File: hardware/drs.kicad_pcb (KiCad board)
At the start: 4 copper layers, 70 x 45 mm, 100 parts, among them IC1 TPS54202HDDCR, J1 USB_C_Receptacle_USB2.0_16P, J2 FTSH-107-01-L-D-K, J3 POWER & CAN & SPI2, J4 PWM1, J5 PWM2, Q1 SI2347DS-T1-GE3, Q2 LMR51635XDDCR, Q3 LMR51635XDDCR, T1 TP_VCC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

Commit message: pcb can & usb update
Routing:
- net /Control/NRST: track 14.9 -> 16.3 mm
- net /Connectors/TX: track 19.0 -> 20.5 mm
- net GND: track 27.6 -> 26.5 mm

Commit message: pcb update
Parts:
- moved J3 13.4 mm to (141.8, 74.8), turned to 180 degrees
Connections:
- J3 pad 10: /Connectors/SCK -> CAN_P
- J3 pad 11: GND -> unconnected-(J3-Pin_11-Pad11)
- J3 pad 12: GND -> CAN_N
- J3 pad 3: +6V6S1 -> GND
- J3 pad 4: CAN_L -> GND
- J3 pad 5: +6V6S2 -> /Connectors/SCK
- J3 pad 6: CAN_H -> /Connectors/MISO
- J3 pad 7: /Connectors/MISO -> unconnected-(J3-Pin_7-Pad7)
- J3 pad 8: unconnected-(J3-Pin_8-Pad8) -> /Connectors/MOSI
- J3 pad 9: /Connectors/MOSI -> unconnected-(J3-Pin_9-Pad9)
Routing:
- net VCC: track 29.7 -> 13.2 mm
- net /Power/VCC_IN: track 39.7 -> 40.8 mm

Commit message: pcb update
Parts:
- moved J4 0.25 mm to (164.4, 73.0)
- turned D6 to 0 degrees
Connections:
- D8 pad 1: /CAN/CAN_N -> CAN_N
- D8 pad 2: /CAN/CAN_P -> CAN_P
- JP1 pad 1: /CAN/CAN_P -> CAN_P
- R17 pad 2: /CAN/CAN_N -> CAN_N
- T15 pad 1: /CAN/CAN_P -> CAN_P
- T16 pad 1: /CAN/CAN_N -> CAN_N
- U3 pad 6: /CAN/CAN_N -> CAN_N
- U3 pad 7: /CAN/CAN_P -> CAN_P
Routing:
- net /Connectors/PWM2: track 0.00 -> 74.5 mm, vias 0 -> 1
- net /Connectors/PWM1: track 0.00 -> 67.7 mm, vias 0 -> 1
- net /Connectors/SCK: track 0.00 -> 50.5 mm, vias 0 -> 1
- net /Connectors/MISO: track 0.00 -> 49.4 mm, vias 0 -> 1
- net /Connectors/MOSI: track 0.00 -> 47.1 mm, vias 0 -> 1
- net +5V: track 13.4 -> 58.6 mm
- net VBUS: track 0.00 -> 30.0 mm
- net CAN_P: track 0.00 -> 30.0 mm
- net /Connectors/DIO: track 0.00 -> 25.4 mm, vias 0 -> 4
- net CAN_N: track 0.00 -> 24.2 mm
- net /Power/+6V6S2_OUT: track 0.00 -> 17.2 mm, vias 0 -> 2
- net /Power/+6V6S1_OUT: track 0.00 -> 17.0 mm, vias 0 -> 2
- net /CAN/CAN_N: track 10.2 -> 0.00 mm
- net /CAN/CAN_P: track 10.2 -> 0.00 mm
- net /CAN/RXD: track 20.1 -> 13.8 mm, vias 0 -> 2
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- added copper zone on In2.Cu, net +3V3
- removed copper zone on In2.Cu, net GND

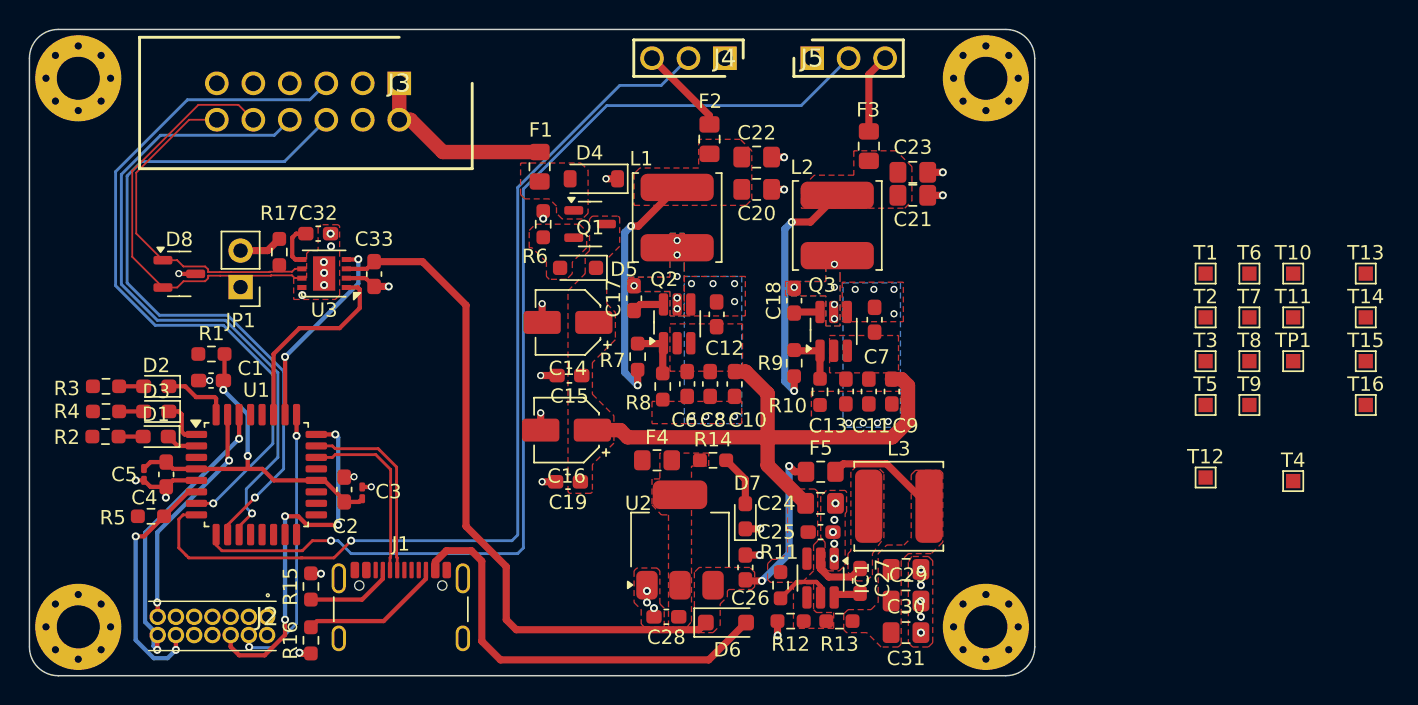
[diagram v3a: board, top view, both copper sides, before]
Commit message: pcb update - testpoints & 3V3
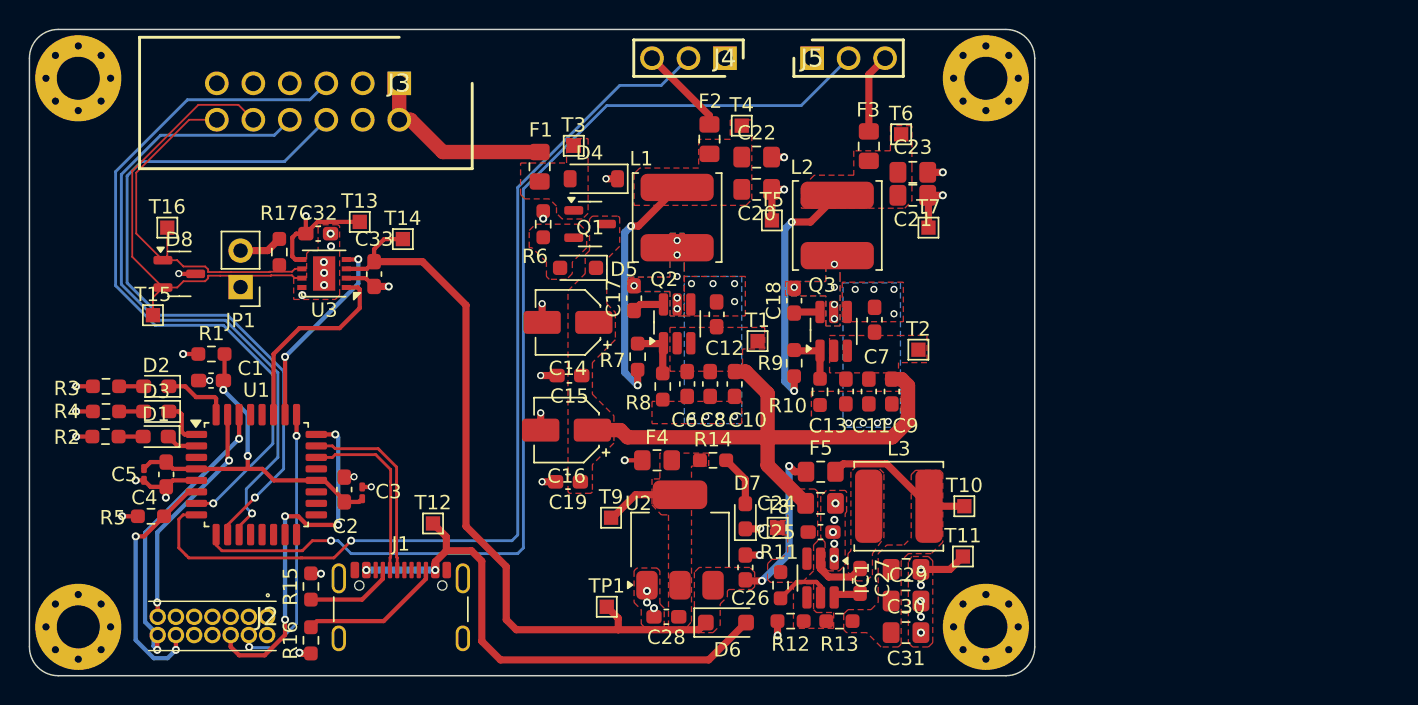
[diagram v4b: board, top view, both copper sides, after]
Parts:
- moved T15 84.5 mm to (124.6, 90.9)
- moved T16 84.4 mm to (125.6, 84.8)
- moved T13 70.1 mm to (139.0, 84.4)
- moved T14 67.3 mm to (142.0, 85.6)
- moved T12 53.9 mm to (144.1, 105.4)
- moved TP1 50.8 mm to (156.2, 111.2)
- moved T3 46.5 mm to (153.9, 79.1)
- moved T4 45.7 mm to (165.6, 77.7)
- moved T9 45.1 mm to (156.5, 105.0)
- moved T8 34.8 mm to (168.1, 105.7)
- moved T5 32.8 mm to (167.7, 84.3)
- moved T1 31.6 mm to (166.7, 92.7)
- moved T11 28.4 mm to (181.0, 107.7)
- moved T10 28.1 mm to (181.1, 104.2)
- moved T6 26.1 mm to (176.7, 78.3)
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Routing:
- net +3V3: track 3.12 -> 15.3 mm, vias 0 -> 7
- net GND: track 26.2 -> 33.9 mm
- net VBUS: track 30.0 -> 37.1 mm, vias 0 -> 2
- net /Power/VO_+3.3V: track 0.00 -> 5.46 mm
- net +5V: track 58.6 -> 63.6 mm
- net /Power/+5V_OUT: track 7.96 -> 10.4 mm
- net CAN_N: track 24.2 -> 26.6 mm
- net CAN_P: track 30.0 -> 32.2 mm

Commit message: pcb update
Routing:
- net GND: track 33.9 -> 36.6 mm, vias 57 -> 54
- net /Connectors/DIO: track 25.4 -> 27.4 mm
- net /Control/NRST: track 17.3 -> 18.8 mm
- net /Connectors/CLK: track 19.4 -> 20.6 mm
- net /Connectors/TX: track 20.5 -> 21.5 mm
- net /Power/SW_+6V6S1: vias 6 -> 5

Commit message: pcb update
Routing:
- net /Connectors/D-: track 12.7 -> 15.1 mm
- net /Connectors/D+: track 13.4 -> 15.1 mm
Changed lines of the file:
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@@
 			(pinfunction "13")
 			(pintype "passive")
-			(clearance 0.15)
 		)
 		(pad "14" thru_hole circle
@@
 			(pinfunction "14")
 			(pintype "passive")
-			(clearance 0.15)
 		)
 		(embedded_fonts no)
@@
 	)
 	(segment
+		(start 142.321508 107.782499)
+		(end 141.60901 107.782499)
+		(width 0.215)
+		(layer "F.Cu")
+		(net 17)
+	)
+	(segment
 		(start 137.292501 100.1925)
 		(end 140.28595 100.1925)
@@
 	)
 	(segment
+		(start 142.60901 108.070001)
+		(end 142.321508 107.782499)
+		(width 0.215)
+		(layer "F.Cu")
+		(net 17)
+	)
+	(segment
 		(start 140.381718 100.288268)
 		(end 141.56651 101.47306)
@@
 	)
 	(segment
+		(start 142.60901 108.645)
+		(end 142.60901 108.070001)
+		(width 0.215)
+		(layer "F.Cu")
+		(net 17)
+	)
+	(segment
 		(start 135.975 100)
 		(end 137.100001 100)
@@
 	)
 	(segment
+		(start 141.29601 109.4785)
+		(end 141.10901 109.2915)
+		(width 0.215)
+		(layer "F.Cu")
+		(net 18)
+	)
+	(segment
 		(start 141.15151 101.64496)
 		(end 141.15151 102.486843)
@@
 	)
 	(segment
+		(start 142.10901 109.19372)
+		(end 141.82423 109.4785)
+		(width 0.215)
+		(layer "F.Cu")
+		(net 18)
+	)
+	(segment
 		(start 140.11405 100.6075)
 		(end 141.15151 101.64496)
@@
 		(layer "F.Cu")
 		(net 18)
+	)
+	(segment
+		(start 142.10901 108.645)
+		(end 142.10901 109.19372)
+		(width 0.215)
+		(layer "F.Cu")
+		(net 18)
+	)
+	(segment
+		(start 141.82423 109.4785)
+		(end 141.29601 109.4785)
+		(width 0.215)
+		(layer "F.Cu")
+		(net 18)
+	)
+	(segment
+		(start 141.10901 109.2915)
+		(end 141.10901 108.645)
+		(width 0.215)
+		(layer "F.Cu")
+		(net 18)
